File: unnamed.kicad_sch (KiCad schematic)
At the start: 29 parts, among them J1 C128990, J2 C128990, SW1 KeySwitch, SW10 KeySwitch, SW11 KeySwitch, SW12 KeySwitch, SW13 KeySwitch, SW14 KeySwitch, SW15 KeySwitch, SW16 KeySwitch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

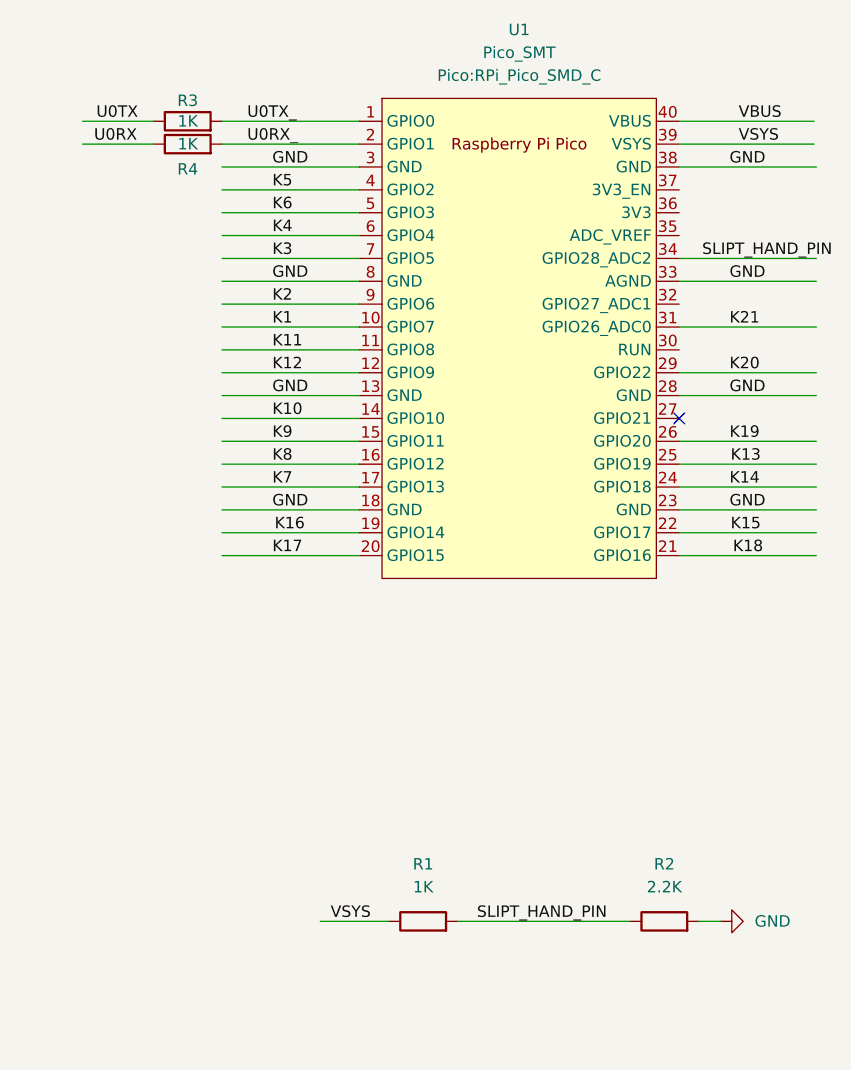
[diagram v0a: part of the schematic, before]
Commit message: update switch footprint, change 0805 to hand-solder footprint, update schematic value.
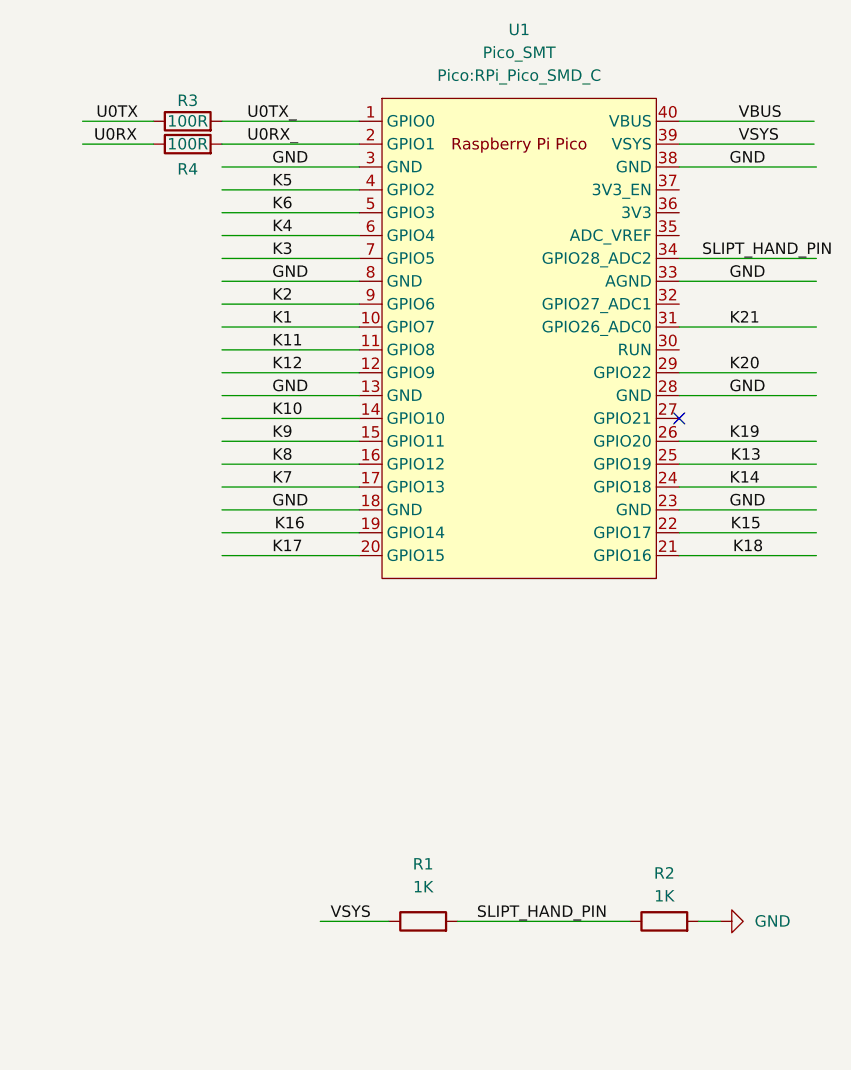
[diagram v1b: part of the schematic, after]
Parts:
- R1: footprint Resistor_SMD:R_0805_2012Metric -> Resistor_SMD:R_0805_2012Metric_Pad1.20x1.40mm_HandSolder
- R2: value 2.2K -> 1K; footprint Resistor_SMD:R_0805_2012Metric -> Resistor_SMD:R_0805_2012Metric_Pad1.20x1.40mm_HandSolder
- R3, R4: value 1K -> 100R; footprint Resistor_SMD:R_0805_2012Metric -> Resistor_SMD:R_0805_2012Metric_Pad1.20x1.40mm_HandSolder
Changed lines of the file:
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@@
       (effects (font (size 1.27 1.27)))
     )
-    (property "Value" "1K" (at 159.004 45.974 90)
-      (effects (font (size 1.27 1.27)))
-    )
-    (property "Footprint" "Resistor_SMD:R_0805_2012Metric" (at 159.004 47.752 90)
+    (property "Value" "100R" (at 159.004 45.974 90)
+      (effects (font (size 1.27 1.27)))
+    )
+    (property "Footprint" "Resistor_SMD:R_0805_2012Metric_Pad1.20x1.40mm_HandSolder" (at 159.004 47.752 90)
       (effects (font (size 1.27 1.27)) hide)
     )
@@
       (effects (font (size 1.27 1.27)))
     )
-    (property "Footprint" "Resistor_SMD:R_0805_2012Metric" (at 185.166 136.652 90)
+    (property "Footprint" "Resistor_SMD:R_0805_2012Metric_Pad1.20x1.40mm_HandSolder" (at 185.166 136.652 90)
       (effects (font (size 1.27 1.27)) hide)
     )
@@
       (effects (font (size 1.27 1.27)))
     )
-    (property "Value" "1K" (at 159.004 48.514 90)
-      (effects (font (size 1.27 1.27)))
-    )
-    (property "Footprint" "Resistor_SMD:R_0805_2012Metric" (at 159.004 50.292 90)
+    (property "Value" "100R" (at 159.004 48.514 90)
+      (effects (font (size 1.27 1.27)))
+    )
+    (property "Footprint" "Resistor_SMD:R_0805_2012Metric_Pad1.20x1.40mm_HandSolder" (at 159.004 50.292 90)
       (effects (font (size 1.27 1.27)) hide)
     )
@@
   (symbol (lib_id "Device:R") (at 211.963 134.874 90) (unit 1)
     (in_bom yes) (on_board yes) (dnp no) (fields_autoplaced)
-    (property "Reference" "R2" (at 211.963 128.524 90)
-      (effects (font (size 1.27 1.27)))
-    )
-    (property "Value" "2.2K" (at 211.963 131.064 90)
-      (effects (font (size 1.27 1.27)))
-    )
-    (property "Footprint" "Resistor_SMD:R_0805_2012Metric" (at 211.963 136.652 90)
-      (effects (font (size 1.27 1.27)) hide)
-    )
+    (property "Reference" "R2" (at 211.963 129.54 90)
+      (effects (font (size 1.27 1.27)))
+    )
+    (property "Value" "1K" (at 211.963 132.08 90)
+      (effects (font (size 1.27 1.27)))
+    )
+    (property "Footprint" "Resistor_SMD:R_0805_2012Metric_Pad1.20x1.40mm_HandSolder" (at 211.963 136.652 90)
+      (effects (font (size 1.27 1.27)) hide)
+    )
